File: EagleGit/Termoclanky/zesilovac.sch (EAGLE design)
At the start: 94 parts, among them IC1 TL061P, IC2 TL061P, IC3 TL061P, IC4 TL061P, Q1 BD140, Q2 BD140, Q3 BD140, Q4 BD140, T1 BD139, T2 BD139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

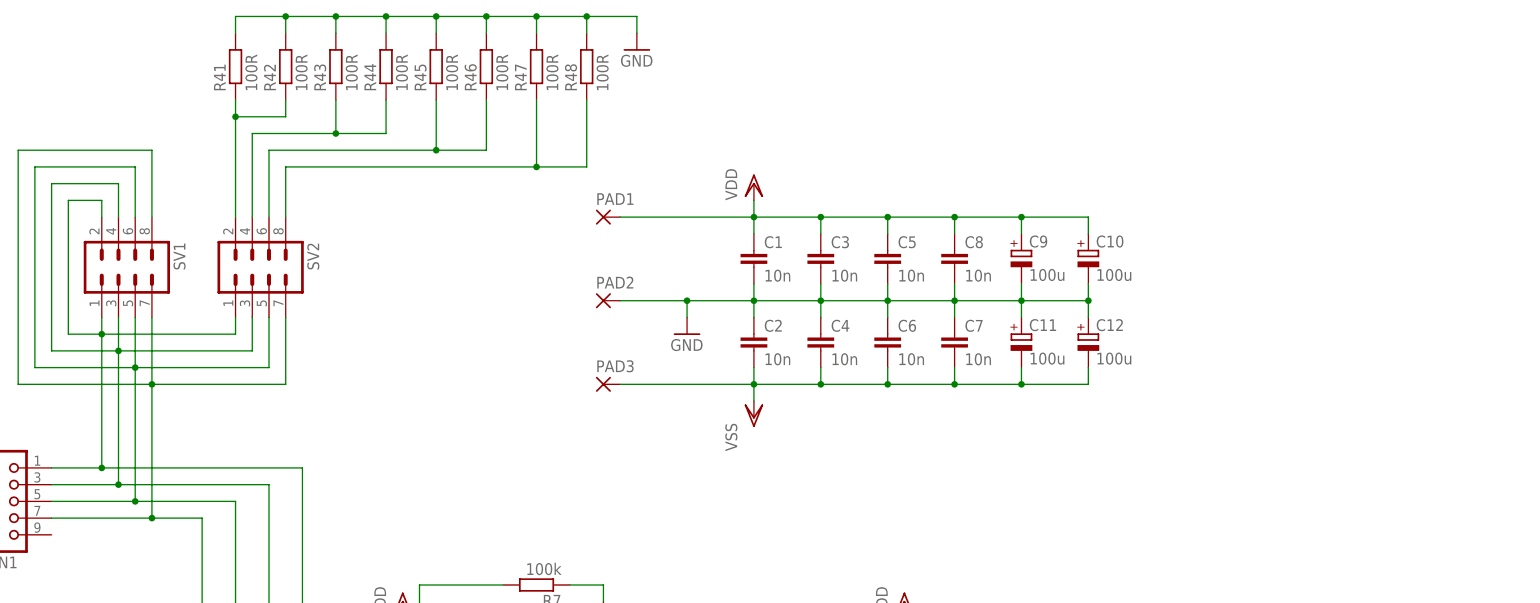
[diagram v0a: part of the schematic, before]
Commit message: Rozdeleni vstupnich 50 ohmovych odporu k jednotlivym vstupum.
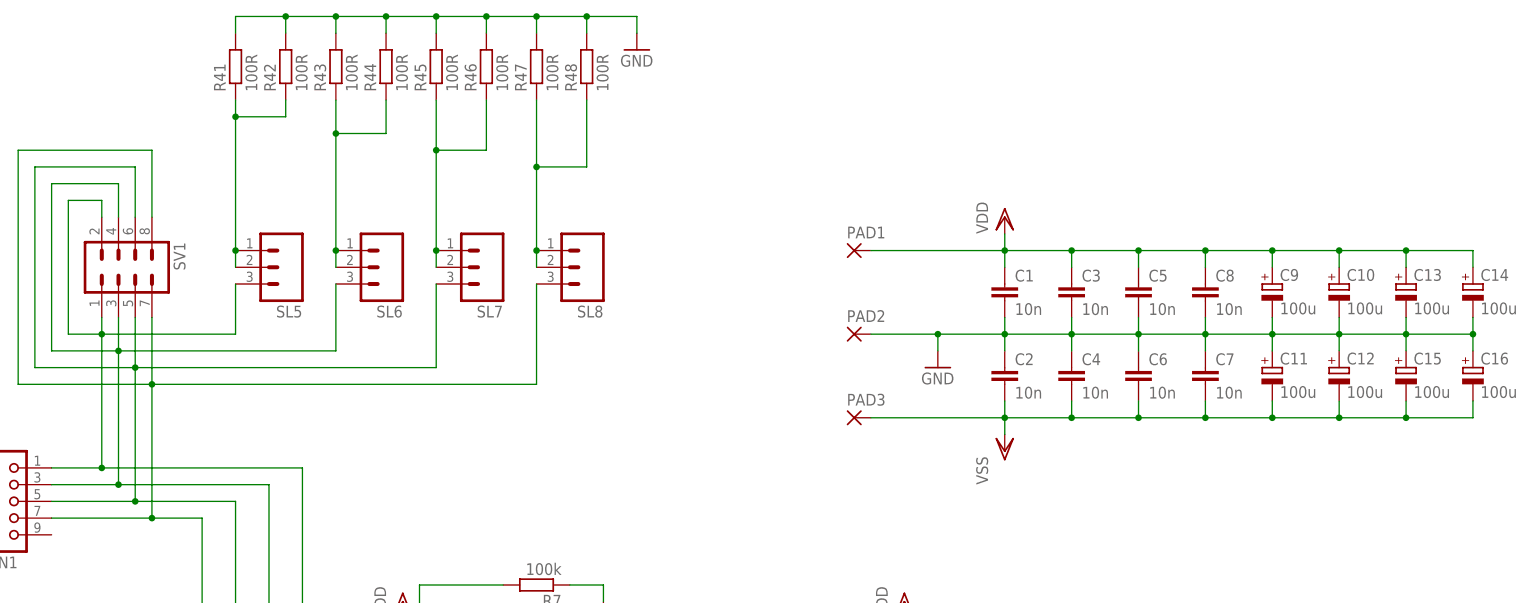
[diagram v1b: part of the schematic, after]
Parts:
- removed SV2: (no value), con-lstb:MA04-2
- added C13, C14, C15, C16: 100u, rcl:CPOL-EUE5-13
- added SL5, SL6, SL7, SL8: (no value), con-amp-quick:M03
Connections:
- removed net N$41: R41.1, R42.1, SV2.2
- new net N$47: R41.1, R42.1, SL5.1, SL5.2
- net GND: now also C13.-, C14.-, C15.+, C16.+
- net N$14: now also SL6.3; no longer SV2.3
- net N$22: now also SL7.3; no longer SV2.5
- net N$30: now also SL8.3; no longer SV2.7
- net N$42: now also SL6.1, SL6.2; no longer SV2.4
- net N$43: now also SL7.1, SL7.2; no longer SV2.6
- net N$44: now also SL8.1, SL8.2; no longer SV2.8
- net N$6: now also SL5.3; no longer SV2.1
- net VDD: now also C13.+, C14.+
- net VSS: now also C15.-, C16.-
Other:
- moved on the sheet: C1, C10, C11, C12, C2, C3, C4, C5, C6, C7, C8, C9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

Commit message: Nova koncepce koncoveho zesilovace podle Papeze. Je treba dodelat totez pro ostatni vstupy.
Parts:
- added R53, R54: 220R, resistor:R-EU_0207/12
- added R55, R56: 1k5, resistor:R-EU_0207/12
- added R57, R58: 4R7, resistor:R-EU_0207/12
- added R59: 5k, pot:TRIM_EU-LI10
- added T5: BD139, transistor-power:BD139
- Q1: device transistor-pnp:BD140 -> transistor-power:BD140
- R49: value 10k -> 1k5
- T1: device transistor:BD139 -> transistor-power:BD139
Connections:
- new net N$41: Q1.B, R54.2, R56.1, R59.A, T5.E
- new net N$49: R53.1, R55.1, R59.E, T1.B, T5.C
- new net N$51: R57.1, T1.E
- new net N$52: Q1.E, R58.2
- new net N$53: R59.S, T5.B
- net N$3: now also R53.2, R54.1; no longer Q1.B, T1.B
- net N$46: now also R57.2, R58.1; no longer Q1.E, T1.E
- net VDD: now also R55.2
- net VSS: now also R56.2
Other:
- moved on the sheet: IC2, IC3, IC4, Q2, Q3, Q4, R10, R12, R13, R14, R15, R16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

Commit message: Termoclanky: Hotovy navrh dps zesilovacu.
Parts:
- added C17, C18, C19, C20, C21, C22, C23, C24: 10n, capacitor-wima:C5/5
- added R60, R61, R67, R68, R74, R75: 4R7, resistor:R-EU_0207/12
- added R62, R64, R69, R70, R76, R77: 1k5, resistor:R-EU_0207/12
- added R63, R65, R71, R72, R78, R79: 220R, resistor:R-EU_0207/12
- added R66, R73, R80: 5k, pot:TRIM_EU-LI10
- added T6, T7, T8: BD139, transistor-power:BD139
- Q2, Q3, Q4: device transistor-pnp:BD140 -> transistor-power:BD140
- R50, R51, R52: value 10k -> 1k5
- T2, T3, T4: device transistor:BD139 -> transistor-power:BD139
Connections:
- new net N$54: R67.1, T3.E
- new net N$55: Q2.E, R61.2
- new net N$56: Q3.E, R68.2
- new net N$57: R60.1, T2.E
- new net N$58: Q2.B, R62.1, R63.2, R66.A, T6.E
- new net N$59: R64.1, R65.1, R66.E, T2.B, T6.C
- new net N$60: R66.S, T6.B
- new net N$61: R69.1, R71.1, R73.E, T3.B, T7.C
- new net N$62: Q3.B, R70.1, R72.2, R73.A, T7.E
- new net N$63: R74.1, T4.E
- new net N$64: Q4.E, R75.2
- new net N$65: R73.S, T7.B
- new net N$68: R76.1, R79.1, R80.E, T4.B, T8.C
- new net N$69: Q4.B, R77.1, R78.2, R80.A, T8.E
- new net N$70: R80.S, T8.B
- net GND: now also C17.2, C18.2, C19.2, C20.2, C21.1, C22.1, C23.1, C24.1
- net N$10: now also R74.2, R75.1; no longer Q4.E, T4.E
- net N$18: now also R67.2, R68.1; no longer Q3.E, T3.E
- net N$26: now also R60.2, R61.1; no longer Q2.E, T2.E
- net N$45: now also R63.1, R65.2; no longer Q2.B, T2.B
- net N$48: now also R71.2, R72.1; no longer Q3.B, T3.B
- net N$50: now also R78.1, R79.2; no longer Q4.B, T4.B
- net VDD: now also C17.1, C18.1, C19.1, C20.1, R64.2, R69.2, R76.2
- net VSS: now also C21.2, C22.2, C23.2, C24.2, R62.2, R70.2, R77.2
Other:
- moved on the sheet: IC2, IC3, IC4, R10, R12, R13, R14, R15, R16, R17, R18, R19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

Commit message: Termistory: - predelany zakoncovaci rezistory na vetsi vykony - rozsireny cesty - finalni verze DPS
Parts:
- removed CON1: (no value), con-harting:CON10
- added R81, R82, R83, R84: 680R, resistor:R-EU_0207/12
- added SV2: (no value), con-lstb:MA05-2
- R29, R30, R31, R32, R33, R34, R35, R36: value 100R -> 27R; device resistor:R-EU_0207/12 -> resistor:R-EU_0411/12
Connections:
- new net N$66: R30.1, R81.1, X1.1
- new net N$67: R32.1, R82.1, X2.1
- new net N$72: R33.1, R34.2
- new net N$73: R34.1, R83.1, X3.1
- net GND: now also R81.2, R82.2, R83.2, R84.2, SV2.10, SV2.2, SV2.4, SV2.6, SV2.8; no longer CON1.2, CON1.4, CON1.6, CON1.8
- net N$10: no longer R36.2
- net N$14: now also SV2.3; no longer CON1.3
- net N$18: no longer R34.2
- net N$22: now also SV2.5; no longer CON1.5
- net N$26: no longer R32.2
- net N$30: now also SV2.7; no longer CON1.7
- net N$36: now also R30.2; no longer R30.1, X1.1
- net N$37: now also R32.2; no longer R32.1, X2.1
- net N$38: now also R35.1, R36.2; no longer R33.1, R34.1, X3.1
- net N$39: now also R84.1; no longer R35.1
- net N$46: no longer R30.2
- net N$6: now also SV2.1; no longer CON1.1
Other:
- moved on the sheet: R30, R32, R34, R36, X1, X2, X3, X4
